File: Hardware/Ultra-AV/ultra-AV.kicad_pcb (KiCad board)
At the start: 2 copper layers, 72.2 x 35 mm, 16 parts, among them J1 Conn_01x04, J11 TC_1578891_SCART, J2 Conn_01x04, J3 Conn_01x04, J4 Conn_01x04, J5 Conn_01x04, J6 Conn_RCJ-023, J7 Conn_RCJ-022, J9 NorComp_111-014-213L001

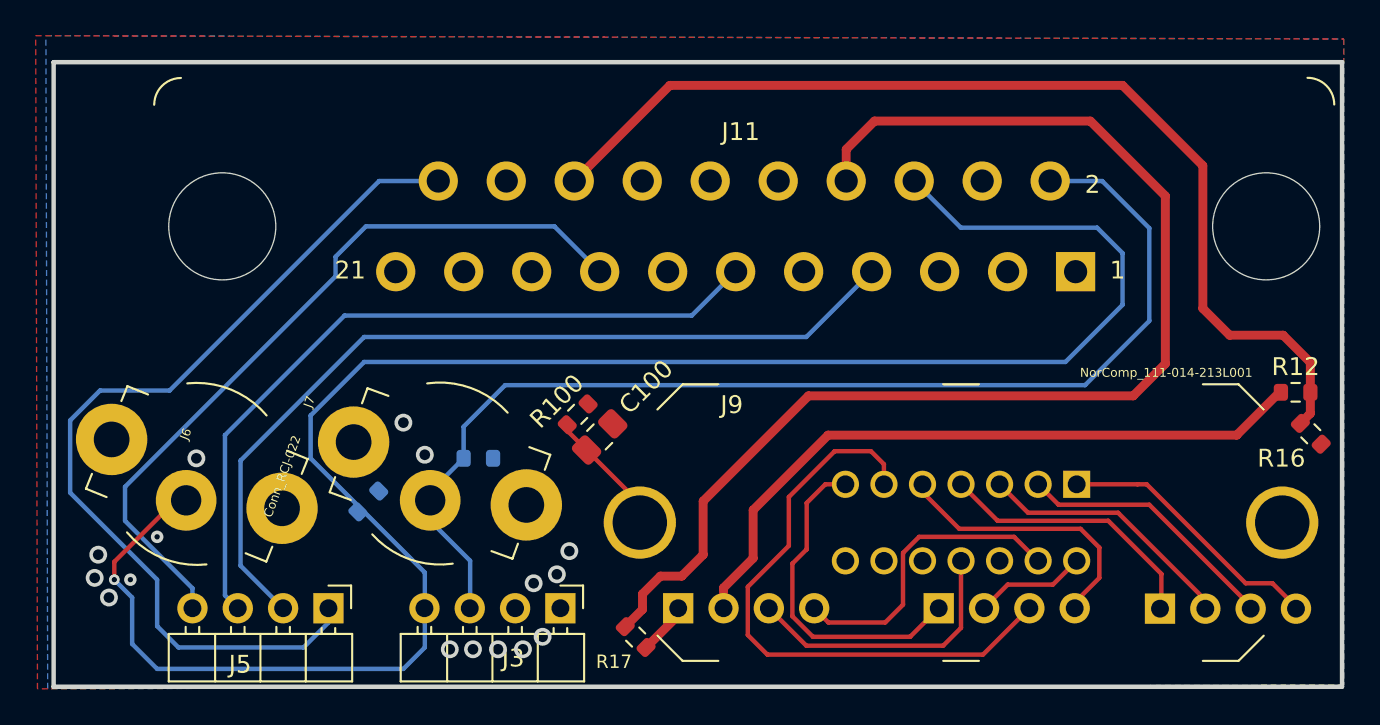
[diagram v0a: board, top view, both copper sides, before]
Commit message: Redesigned VDP-board to include a socket, increased it to 4 layers. Various clean-ups here and there. Improved the printer-port and joystick-port 3D-models. Improved the cooling-fin 3D-model, and added attachment-spring in 3D-model.
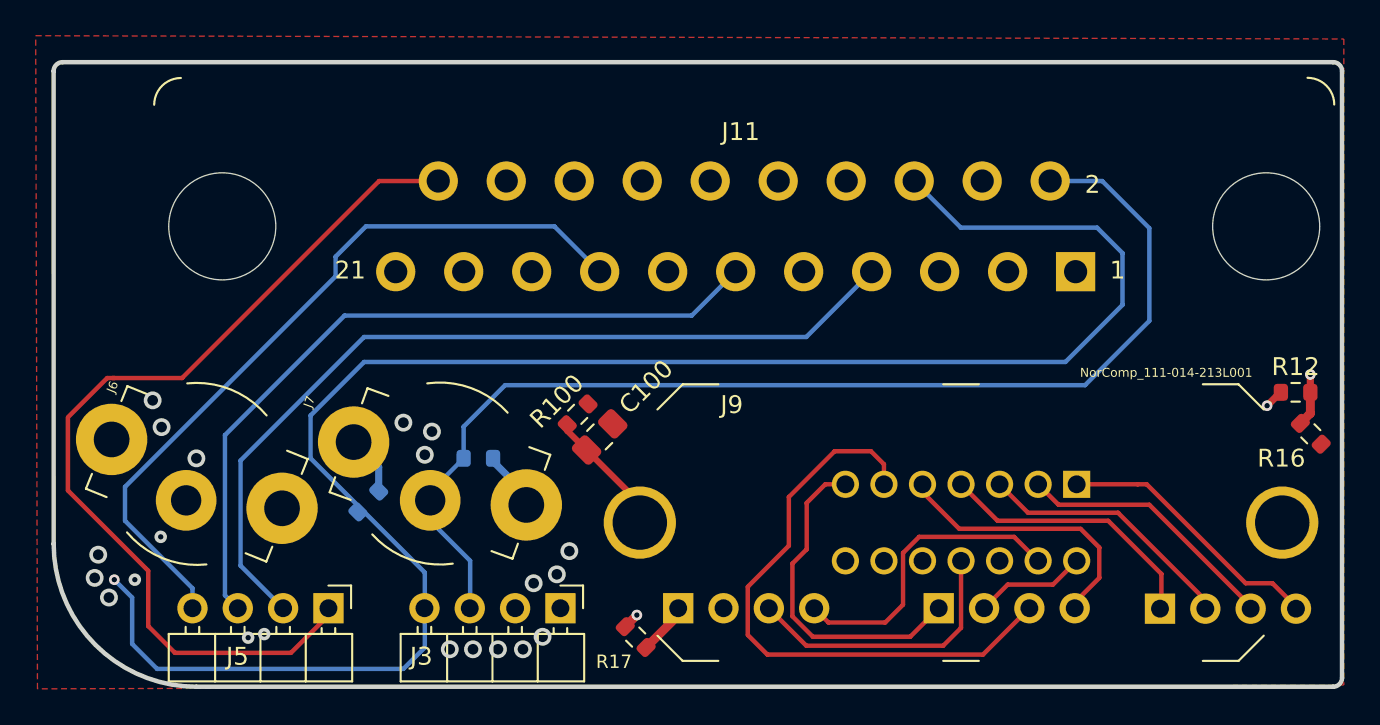
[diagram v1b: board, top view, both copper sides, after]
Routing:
- net GNDA: track 0.00 -> 6.71 mm
- net /AUD_R: track 63.3 -> 64.6 mm
- net /CSYNC: track 51.2 -> 51.8 mm
- net /+12V-1K: track 70.1 -> 70.2 mm, vias 0 -> 1
- net +5V: vias 0 -> 1
- net /2.5V: vias 0 -> 1
- added copper zone on In1.Cu, net GNDA
- removed copper zone on B.Cu, net GNDA
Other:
- outline, holes or cut-outs redrawn
- copper layers 2 -> 4
- rule pad_to_mask_clearance: 0 -> 0.06

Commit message: Generated first PDF-files
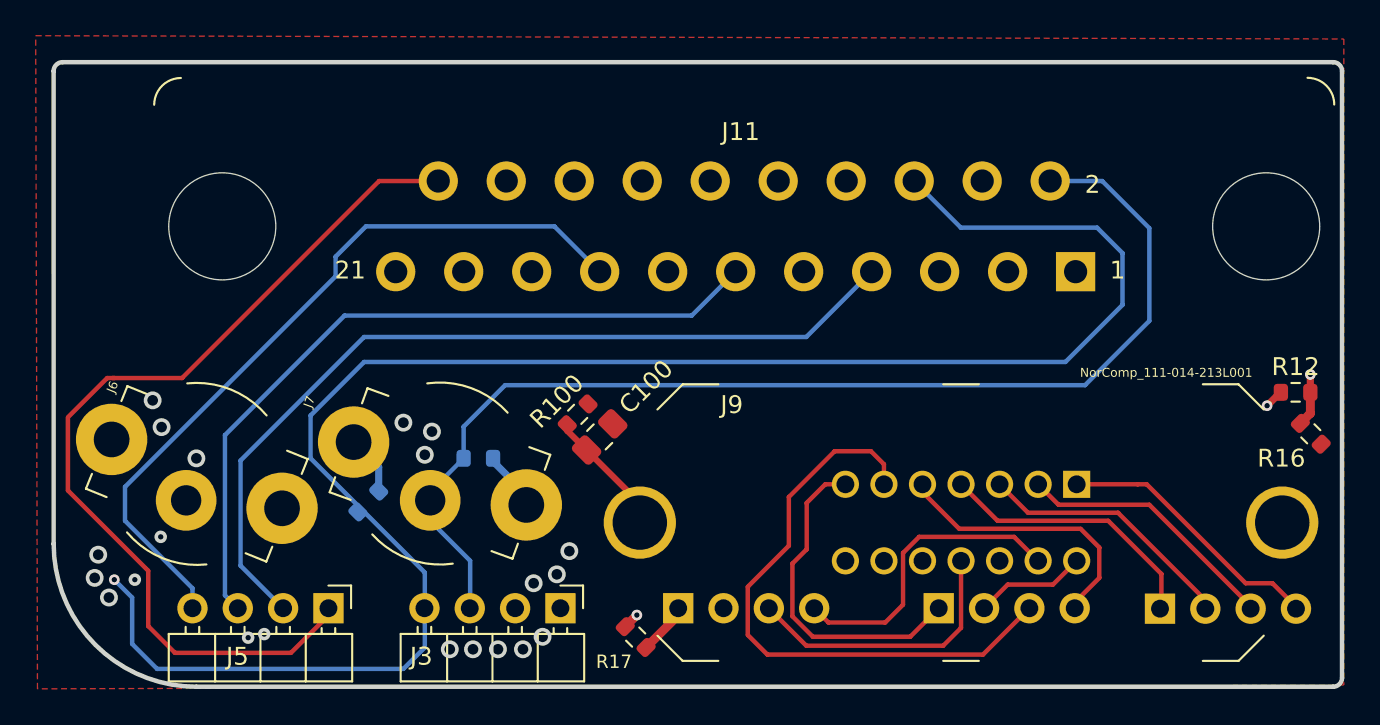
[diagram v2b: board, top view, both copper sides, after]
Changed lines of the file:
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@@
     (thickness 1.999999)
   )
-  (paper "A4")
+  (paper "A3")
   (layers
     (0 "F.Cu" mixed)
@@
     (aux_axis_origin 111.2 111.3)
     (pcbplotparams
-      (layerselection 0x00010fc_ffffffff)
+      (layerselection 0x00310fc_ffffffff)
       (disableapertmacros false)
       (usegerberextensions false)
@@
       (svguseinch false)
       (svgprecision 6)
-      (excludeedgelayer true)
-      (plotframeref false)
+      (excludeedgelayer false)
+      (plotframeref true)
       (viasonmask false)
       (mode 1)
@@
       (sketchpadsonfab false)
       (subtractmaskfromsilk false)
-      (outputformat 1)
+      (outputformat 4)
       (mirror false)
-      (drillshape 1)
+      (drillshape 0)
       (scaleselection 1)
-      (outputdirectory "")
+      (outputdirectory "../../Docs/")
     )
   )
@@
     (fp_line (start 13.9 -7.6) (end 13.9 -4.6) (layer "F.Fab") (width 0.1))
     (fp_arc (start -21.129899 1.979899) (mid -21.95 0) (end -21.129899 -1.979899) (layer "F.Fab") (width 0.1))
-    (fp_arc (start 11.050145 4.254) (mid 10.698968 5.188092) (end 9.878815 5.756603) (layer "F.Fab") (width 0.1))
+    (fp_arc (start 11.050145 4.254) (mid 10.698969 5.188094) (end 9.878815 5.756603) (layer "F.Fab") (width 0.1))
     (fp_arc (start 11.427855 -5.745537) (mid 12.27547 -5.139908) (end 12.6 -4.15) (layer "F.Fab") (width 0.1))
     (fp_arc (start -12.6 -4.15) (mid -12.275468 -5.139907) (end -11.427855 -5.745537) (layer "F.Fab") (width 0.1))
@@
       (effects (font (size 1 1) (thickness 0.15)))
     )
-    (fp_arc (start 31.56434 -8.325) (mid 32.624974 -7.885646) (end 33.06434 -6.825) (layer "F.SilkS") (width 0.12))
+    (fp_arc (start 31.56434 -8.325) (mid 32.62501 -7.885652) (end 33.06434 -6.825) (layer "F.SilkS") (width 0.12))
     (fp_arc (start -33.06434 -6.81434) (mid -32.625 -7.875) (end -31.56434 -8.31434) (layer "F.SilkS") (width 0.12))
     (fp_line (start 33.2 8.55) (end 33.2 -8.5) (layer "F.CrtYd") (width 0.05))
@@
     (fp_line (start 1 -0.625) (end 1 0.625) (layer "F.Fab") (width 0.1))
     (fp_line (start -1 0.625) (end -1 -0.625) (layer "F.Fab") (width 0.1))
-    (pad "1" smd roundrect (at -1.0375 0 45) (size 1.175 1.45) (layers "F.Cu" "F.Paste" "F.Mask") (roundrect_rratio 0.212766)
+    (pad "1" smd roundrect (at -1.0375 0 45) (size 1.175 1.45) (layers "F.Cu" "F.Paste" "F.Mask") (roundrect_rratio 0.2127659574)
       (net 31 "Net-(C100-Pad1)") (pinfunction "1") (pintype "passive"))
-    (pad "2" smd roundrect (at 1.0375 0 45) (size 1.175 1.45) (layers "F.Cu" "F.Paste" "F.Mask") (roundrect_rratio 0.212766)
+    (pad "2" smd roundrect (at 1.0375 0 45) (size 1.175 1.45) (layers "F.Cu" "F.Paste" "F.Mask") (roundrect_rratio 0.2127659574)
       (net 1 "GND") (pinfunction "2") (pintype "passive"))
     (model "${KICAD6_3DMODEL_DIR}/Capacitor_SMD.3dshapes/C_0805_2012Metric.wrl"

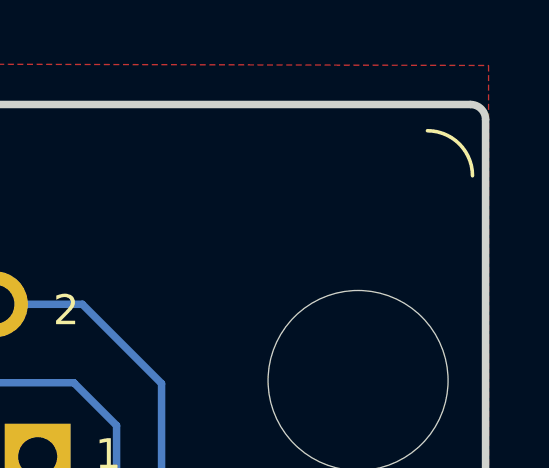
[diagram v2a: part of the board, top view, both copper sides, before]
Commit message: Reworked the Printer-port 3D model, and the Scart 3D-model. Generated a 3D model of the main board. Moved peripheral components from separate expansion-headers, to a singular IO-shield board.
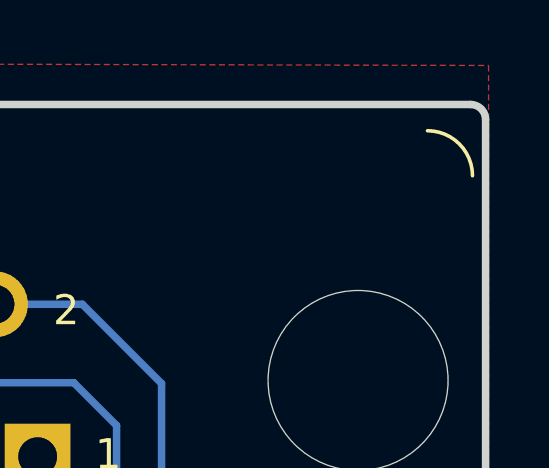
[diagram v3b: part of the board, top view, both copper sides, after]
